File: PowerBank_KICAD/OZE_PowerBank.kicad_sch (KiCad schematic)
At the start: 86 parts, among them IC1 TPS2514ADBVT, IC3 TPS25810RVCR, J1 Conn_01x02_Pin, J10 Conn_01x04_Pin, J11 Conn_01x02_Pin, J12 Battery with BMS Input, J13 Conn_01x10_Pin, J2 DCJ200-10-A-XX-K_REVA, J3 Conn_01x04_Pin, J4 Conn_01x04_Pin, J5 Conn_01x04_Pin, J6 Conn_01x10_Pin, J7 USB_A, J8 USB_C_Receptacle_PowerOnly_6P, J9 Conn_01x04_Pin, Q1 PMOS, Q2 IRLZ44N, Q3 IRLZ44N, SW1 SW_Push, SW2 SW_SPDT, U1 TLV70233_SOT23-5, U2 STM32F103C8Tx, U3 LM5106SD, U5 INA180A2, Y1 16MHz

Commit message: added conectors footprints
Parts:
- added C33: 10u, Capacitor_SMD:C_0805_2012Metric_Pad1.18x1.45mm_HandSolder, symbol Device:C_Small
- added C34, C35: 100n, Capacitor_SMD:C_0805_2012Metric_Pad1.18x1.45mm_HandSolder, symbol Device:C_Small
- added D10: BLUE, LED_SMD:LED_1206_3216Metric_Pad1.42x1.75mm_HandSolder, symbol Device:LED
- added H1, H2, H3, H4: MountingHole, MountingHole:MountingHole_2.2mm_M2_ISO7380, symbol Mechanical:MountingHole
- added J14: Conn_01x04_Pin, symbol Connector:Conn_01x04_Pin
- added J15, J16, J17: Conn_01x04_Pin, Connector_PinSocket_2.54mm:PinSocket_1x04_P2.54mm_Vertical, symbol Connector:Conn_01x04_Pin
- added R17: 1k, Resistor_SMD:R_0805_2012Metric_Pad1.20x1.40mm_HandSolder, symbol Device:R
- added R18, R19, R25: 100k, Resistor_SMD:R_0805_2012Metric_Pad1.20x1.40mm_HandSolder, symbol Device:R
- added R20, R21, R22, R23, R24: 0, Resistor_SMD:R_0805_2012Metric_Pad1.20x1.40mm_HandSolder, symbol Device:R
- J1: footprint (none) -> TerminalBlock_Phoenix:TerminalBlock_Phoenix_PT-1,5-2-5.0-H_1x02_P5.00mm_Horizontal
- J10: footprint (none) -> TerminalBlock_Phoenix:TerminalBlock_Phoenix_PT-1,5-4-5.0-H_1x04_P5.00mm_Horizontal
- J11: footprint (none) -> Connector_JST:JST_XH_B2B-XH-A_1x02_P2.50mm_Vertical
- J13, J6: footprint (none) -> Connector_PinSocket_2.54mm:PinSocket_1x10_P2.54mm_Vertical
- J9: footprint (none) -> TerminalBlock_Phoenix:TerminalBlock_Phoenix_PT-1,5-4-3.5-H_1x04_P3.50mm_Horizontal
- U5: value INA180A2 -> INA180A1
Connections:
- net +12V: now also J17.3 (Pin_3), J17.4 (Pin_4)
- net +3.3V: now also IC3.5 (AUX), C33.1, C34.1, J14.3 (Pin_3), J14.4 (Pin_4), J15.3 (Pin_3), J15.4 (Pin_4), R18.2, R19.2, R25.2
- net +5V: now also J16.3 (Pin_3), J16.4 (Pin_4); no longer IC3.5 (AUX), IC3.6 (EN)
- net ENABLE: now also R20.2; no longer U2.10 (PA0)
- net GND: now also C33.2, C34.2, C35.2, D10.1 (K), J14.1 (Pin_1), J14.2 (Pin_2), J15.1 (Pin_1), J15.2 (Pin_2), J16.1 (Pin_1), J16.2 (Pin_2), J17.1 (Pin_1), J17.2 (Pin_2)
- net I_OUT: now also R24.2; no longer U2.14 (PA4)
- net PWM: now also R21.2; no longer U2.11 (PA1)
- net V_BAT: now also R23.2; no longer U2.13 (PA3)
- net V_beforeBUCK: now also R22.2; no longer U2.12 (PA2)
- net at C25.1, C26.1, C27.1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: now also IC3.15 (OUT-B)
- net at C28.1, C29.1, L1.2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: now also R17.2
- net at C12.1, C14.1, FB1.1: now also C35.1
- net FAULT: now reaches U2.31 (PA10)
- net FAULT: now also IC3.1 (~{FAULT}), R19.1
- net ENABLE_TPS: now reaches U2.32 (PA11)
- net ENABLE_TPS: now also IC3.6 (EN)
- net LD_DET: now reaches U2.33 (PA12)
- net LD_DET: now also IC3.20 (~{LD_DET}), R18.1
- net UFP: now reaches U2.38 (PA15)
- net UFP: now also IC3.19 (~{UFP}), R25.1
- net DM1 renamed D-
- net DP1 renamed D+
- new net: D10.2 (A), R17.1
- new net: R22.1, U2.12 (PA2)
- new net: R24.1, U2.14 (PA4)
- new net: R20.1, U2.10 (PA0)
- new net: R21.1, U2.11 (PA1)
- new net: R23.1, U2.13 (PA3)
- no-connect marks 21 -> 13
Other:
- note added: "1%tolerance"
- note added: "1x 100nF per VDD Pin"
- note added: "Brak UFP może wyłączyć przetwornicę"
- note added: "O Ohm to be modular, in case of failure with STM32"
- note added: "diferential pair"
- note added: "electrolytic or ceracmic?"
- note added: "linie CC bardzo krótkie"
- note added: "termal pad, multiple vias"
- note added: "zabezpieczenie żeby nie spalić portu ADC?"
- note added: "zmień na uniwerslane zielone złącze"
- note removed: "1x 100mF per VDD Pin"
- moved on the sheet: C15, C18, C19, C20, C21, FB1

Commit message: PCB layout
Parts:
- removed C24, C29: 150uF, symbol Device:C_Polarized
- removed Q1: PMOS, symbol Simulation_SPICE:PMOS
- added C21, C28: 865060657011, 865060657011:CAPAE1030X1050N, symbol 865060657011:865060657011
- added Q1: IRLML6402TRPBF, IRLML6402TRPBF:SOT95P237X112-3N, symbol IRLML6402TRPBF:IRLML6402TRPBF
- 100k1, FB1: footprint (none) -> Resistor_SMD:R_0603_1608Metric_Pad0.98x0.95mm_HandSolder
- C11, C3, C6, C7, C8, C9: footprint Capacitor_SMD:C_0805_2012Metric_Pad1.18x1.45mm_HandSolder -> Capacitor_SMD:C_0402_1005Metric
- C13: footprint Capacitor_SMD:C_0603_1608Metric_Pad1.08x0.95mm_HandSolder -> Capacitor_SMD:C_0402_1005Metric
- C15: renamed from C35; footprint Capacitor_SMD:C_0805_2012Metric_Pad1.18x1.45mm_HandSolder -> Capacitor_SMD:C_0402_1005Metric
- C27: renamed from C34; footprint Capacitor_SMD:C_0805_2012Metric_Pad1.18x1.45mm_HandSolder -> Capacitor_SMD:C_0402_1005Metric
- C30: renamed from C32; footprint Capacitor_SMD:C_0805_2012Metric_Pad1.18x1.45mm_HandSolder -> Capacitor_SMD:C_0402_1005Metric
- D4: value 10V -> SZMM3Z10VST1G; footprint Diode_SMD:D_MiniMELF -> Diode_SMD:D_SOD-323
- J10: renamed from J7; footprint (none) -> Connector_USB:USB_A_TE_292303-7_Horizontal
- J17: renamed from J12; footprint (none) -> TerminalBlock_Phoenix:TerminalBlock_Phoenix_PT-1,5-2-5.0-H_1x02_P5.00mm_Horizontal
- J3, J4, J5: footprint (none) -> Connector_PinSocket_2.54mm:PinSocket_1x04_P2.54mm_Vertical
- J6: renamed from J14; footprint (none) -> Connector_PinSocket_2.54mm:PinSocket_1x04_P2.54mm_Vertical
- J9: renamed from J8; footprint (none) -> Connector_USB:USB_C_Receptacle_GCT_USB4125-xx-x-0190_6P_TopMnt_Horizontal
- L1: footprint (none) -> Inductor_SMD:L_Pulse_PA4320
- R15: renamed from R10; footprint Resistor_SMD:R_0805_2012Metric_Pad1.20x1.40mm_HandSolder -> Resistor_SMD:R_0402_1005Metric
- R19: renamed from R25; footprint Resistor_SMD:R_0805_2012Metric_Pad1.20x1.40mm_HandSolder -> Resistor_SMD:R_0402_1005Metric
- R20: renamed from R18; footprint Resistor_SMD:R_0805_2012Metric_Pad1.20x1.40mm_HandSolder -> Resistor_SMD:R_0402_1005Metric
- R21: renamed from R19; footprint Resistor_SMD:R_0805_2012Metric_Pad1.20x1.40mm_HandSolder -> Resistor_SMD:R_0402_1005Metric
- SW1: footprint (none) -> Button_Switch_THT:SW_PUSH-12mm_Wuerth-430476085716
- U3: now not fitted
- Y1: footprint (none) -> LFXTAL071744Reel:LFXTAL071744Reel
- renumbered C15 to C16, C16 to C17, C17 to C18, C22 to C19, C23 to C20, C18 to C22, C19 to C23, C20 to C24, C33 to C25, C21 to C26, C28 to C29, C26 to C31, C27 to C32, C25 to C33, C30 to C34, C31 to C35, D9 to D10, D10 to D8, D8 to D9, IC3 to IC1, IC1 to IC2, J9 to J11, J10 to J12, J15 to J13, J16 to J14, J17 to J15, J11 to J16, J6 to J7, J13 to J8, R2 to R1, R23 to R10, R24 to R11, R7 to R12, R8 to R13, R9 to R14, R11 to R16, R12 to R17, R13 to R18, R3 to R2, R17 to R22, R14 to R23, R15 to R24, R16 to R25, R1 to R3, R20 to R7, R21 to R8, R22 to R9, U5 to U4
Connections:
- net GND: now also C31.1, C21.2 (-), C28.2 (-); no longer C31.2
- net VIN: now also C21.1 (+), Q1.2 (S)
- net VBUS: now reaches C32.1, C33.1, IC1.14 (OUT-A), IC1.15 (OUT-B), IC2.5 (IN), J10.1 (VBUS), J9.A9 (VBUS), J9.B9 (VBUS)
- net VBUS: now also C31.2; no longer C31.1
- net Gate: now reaches D4.2 (A), R12.1
- net Gate: now also Q1.1 (G)
- net at C29.1, L1.2, R22.2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: now also C28.1 (+)
- net DREN: now reaches D3.2 (A2), F1.2
- net DREN: now also Q1.3 (D)
- no-connect marks 13 -> 16
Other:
- note added: "STEP DOWN"
- note added: "STEP UP"
- moved on the sheet: C29, C31, R12

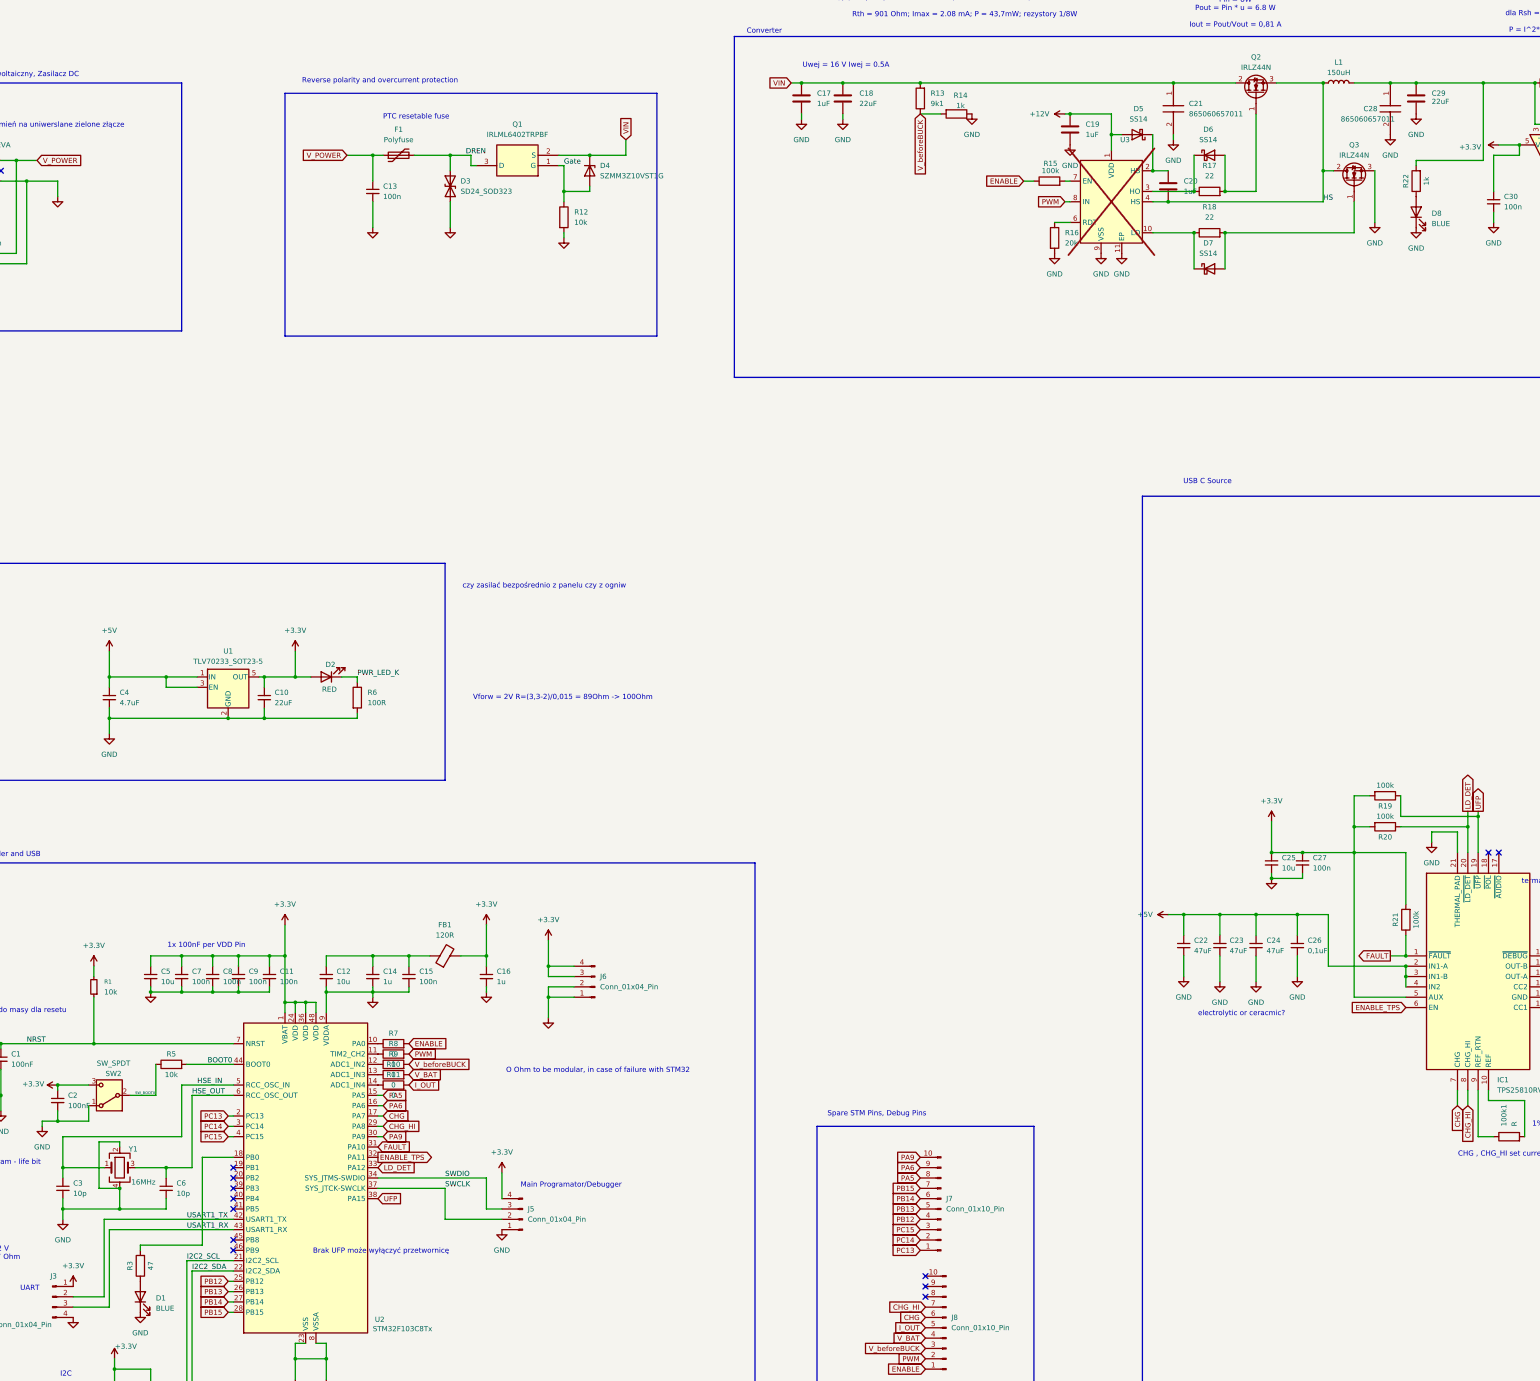
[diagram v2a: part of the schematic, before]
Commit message: 26.11 Hubert - PCB
Poprowadzone ścieżki sygnałowe, prądowe, poza 2 wchodzącymi do sterownika USB-C, USB-A . Brak wylanej masy
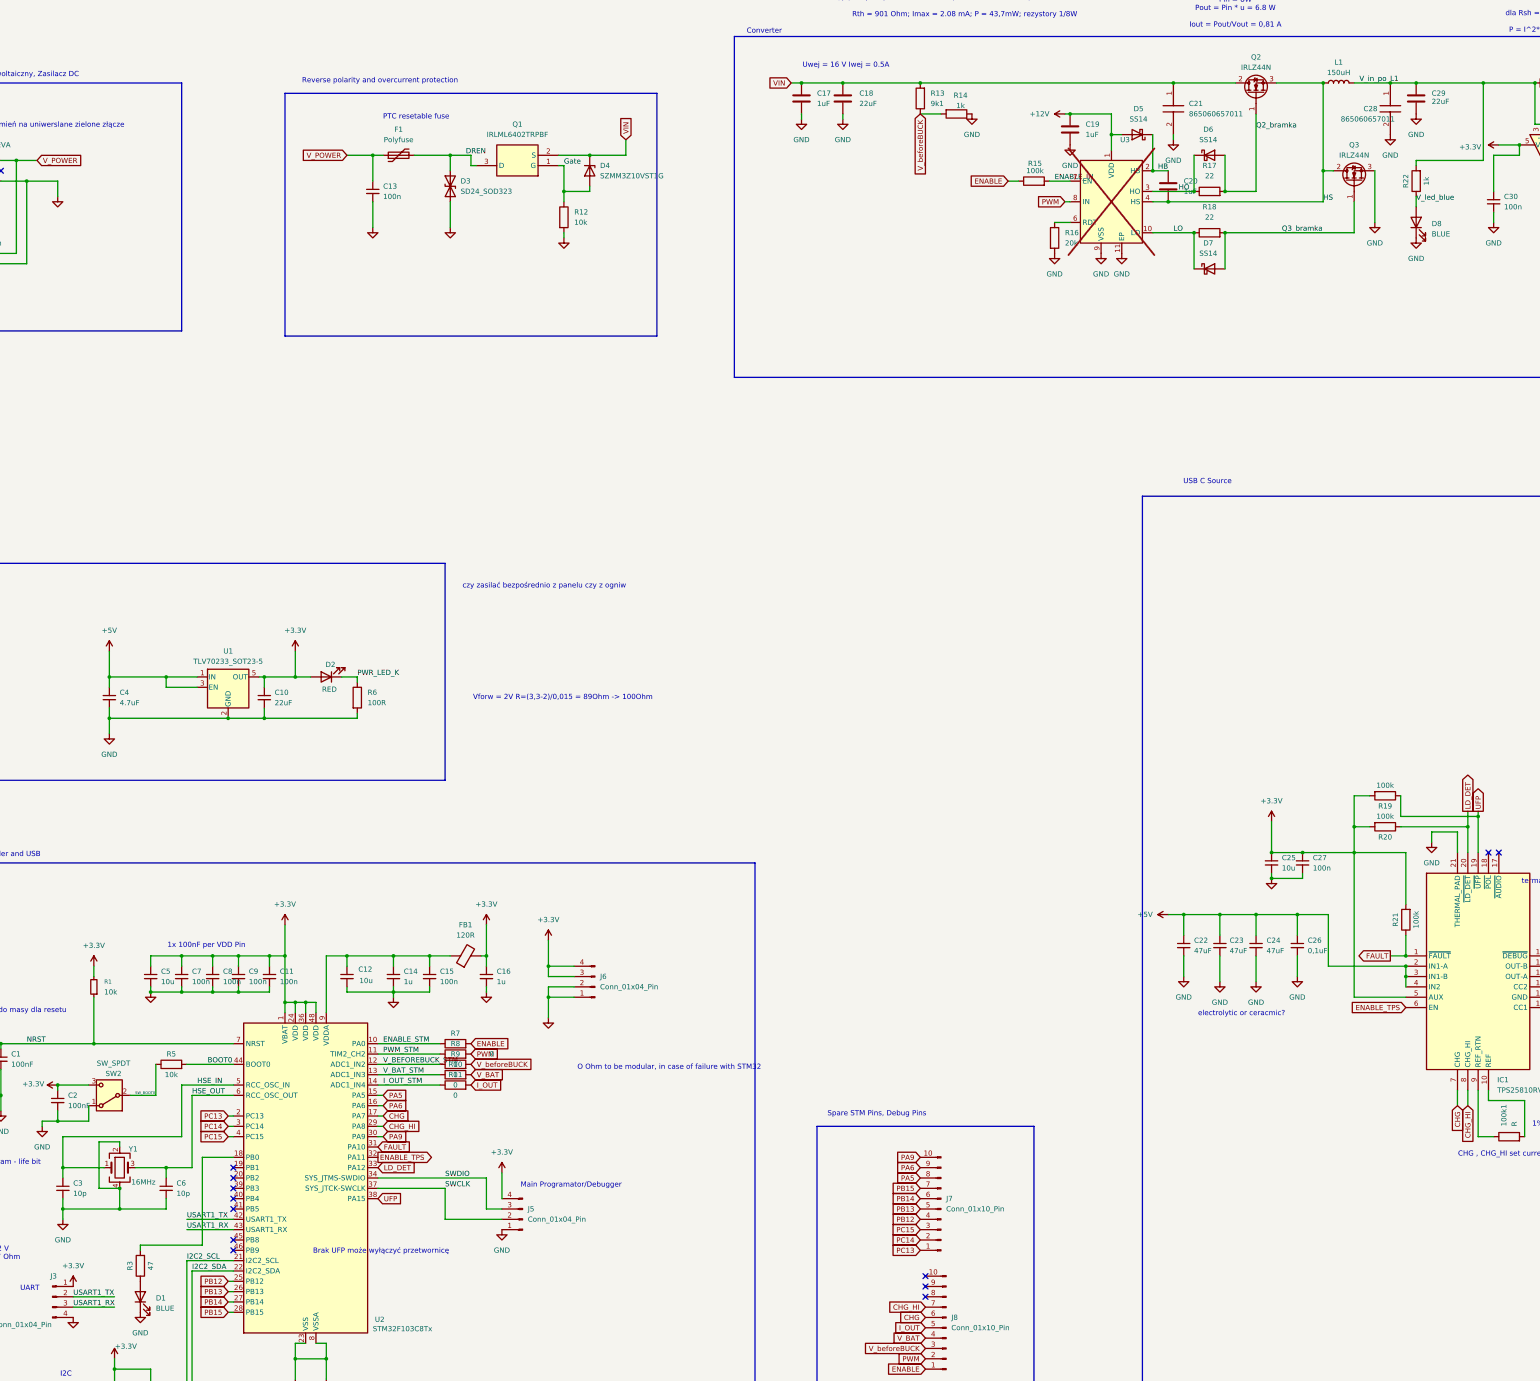
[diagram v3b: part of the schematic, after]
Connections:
- net GND: no longer U2.9 (VDDA)
- net at C12.1, C14.1, C15.1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: now also U2.9 (VDDA)
- net V_led_blue: now reaches D8.2 (A), R22.1
- net HB: now reaches C20.1, D5.1 (K), U3.2 (HB)
- net V_in_po_L1: now reaches C28.1 (+), C29.1, L1.2, R22.2, R23.1, U4.3 (+)
- net Q3_bramka: now reaches D7.2 (A), Q3.1 (G), R18.2
- net HO: now reaches D6.1 (K), R17.1, U3.3 (HO)
- net Q2_bramka: now reaches D6.2 (A), Q2.1 (G), R17.2
- net V_BEFOREBUCK_STM: now reaches R9.1, U2.12 (PA2)
- net I_OUT_STM: now reaches R11.1, U2.14 (PA4)
- net LO: now reaches D7.1 (K), R18.1, U3.10 (LO)
- net ENABLE_IN: now reaches R15.2, U3.7 (EN)
- net ENABLE_STM: now reaches R7.1, U2.10 (PA0)
- net PWM_STM: now reaches R8.1, U2.11 (PA1)
- net V_BAT_STM: now reaches R10.1, U2.13 (PA3)
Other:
- moved on the sheet: C12, C14, C15, D8, FB1, R10, R11, R15, R7, R8, R9

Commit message: changed footprint, correct GND conection to thermal, remove some vias, give additional vias in TPS25810
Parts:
- C1, C2: footprint Capacitor_SMD:C_0805_2012Metric_Pad1.18x1.45mm_HandSolder -> PCM_JLCPCB:C_0805; symbol Device:C_Small -> PCM_JLCPCB-Capacitors:0805,100nF; Attrition Qty (none) -> 10; Capacitance (none) -> 100nF; Category (none) -> Capacitors,Multilayer Ceramic Capacitors MLCC - SMD/SMT; Class (none) -> Basic Component; LCSC (none) -> C28233; Manufacturer (none) -> Samsung Electro-Mechanics; Minimum Qty (none) -> 20; Part (none) -> CL21B104KCFNNNE; Price (none) -> 0.009USD; Process (none) -> SMT; Stock (none) -> 1168020; Temperature Coefficient (none) -> X7R; Tolerance (none) -> ±10%; Voltage Rated (none) -> 100V
- C11, C15, C27, C30, C7, C8, C9: footprint Capacitor_SMD:C_0402_1005Metric -> PCM_JLCPCB:C_0402; symbol Device:C_Small -> PCM_JLCPCB-Capacitors:0402,100nF; Attrition Qty (none) -> 10; Capacitance (none) -> 100nF; Category (none) -> Capacitors,Multilayer Ceramic Capacitors MLCC - SMD/SMT; Class (none) -> Basic Component; LCSC (none) -> C1525; Manufacturer (none) -> Samsung Electro-Mechanics; Minimum Qty (none) -> 20; Part (none) -> CL05B104KO5NNNC; Price (none) -> 0.004USD; Process (none) -> SMT; Stock (none) -> 20208285; Temperature Coefficient (none) -> X7R; Tolerance (none) -> ±10%; Voltage Rated (none) -> 16V
- C12, C25, C31, C32: footprint Capacitor_SMD:C_0805_2012Metric_Pad1.18x1.45mm_HandSolder -> PCM_JLCPCB:C_0805; symbol Device:C_Small -> PCM_JLCPCB-Capacitors:0805,10uF; Attrition Qty (none) -> 10; Capacitance (none) -> 10uF; Category (none) -> Capacitors,Multilayer Ceramic Capacitors MLCC - SMD/SMT; Class (none) -> Basic Component; LCSC (none) -> C15850; Manufacturer (none) -> Samsung Electro-Mechanics; Minimum Qty (none) -> 20; Part (none) -> CL21A106KAYNNNE; Price (none) -> 0.014USD; Process (none) -> SMT; Stock (none) -> 6525809; Temperature Coefficient (none) -> X5R; Tolerance (none) -> ±10%; Voltage Rated (none) -> 25V
- C13: footprint Capacitor_SMD:C_0402_1005Metric -> Capacitor_SMD:C_0805_2012Metric
- C14, C16, C26, C33: footprint Capacitor_SMD:C_0805_2012Metric_Pad1.18x1.45mm_HandSolder -> PCM_JLCPCB:C_0805; symbol Device:C_Small -> PCM_JLCPCB-Capacitors:0805,1uF; Attrition Qty (none) -> 10; Capacitance (none) -> 1uF; Category (none) -> Capacitors,Multilayer Ceramic Capacitors MLCC - SMD/SMT; Class (none) -> Basic Component; LCSC (none) -> C28323; Manufacturer (none) -> Samsung Electro-Mechanics; Minimum Qty (none) -> 20; Part (none) -> CL21B105KBFNNNE; Price (none) -> 0.012USD; Process (none) -> SMT; Stock (none) -> 4334256; Temperature Coefficient (none) -> X7R; Tolerance (none) -> ±10%; Voltage Rated (none) -> 50V
- C17, C19: footprint Capacitor_SMD:C_0805_2012Metric_Pad1.18x1.45mm_HandSolder -> PCM_JLCPCB:C_0805; symbol Device:C -> PCM_JLCPCB-Capacitors:0805,1uF; Attrition Qty (none) -> 10; Capacitance (none) -> 1uF; Category (none) -> Capacitors,Multilayer Ceramic Capacitors MLCC - SMD/SMT; Class (none) -> Basic Component; LCSC (none) -> C28323; Manufacturer (none) -> Samsung Electro-Mechanics; Minimum Qty (none) -> 20; Part (none) -> CL21B105KBFNNNE; Price (none) -> 0.012USD; Process (none) -> SMT; Stock (none) -> 4334256; Temperature Coefficient (none) -> X7R; Tolerance (none) -> ±10%; Voltage Rated (none) -> 50V
- C3, C6: footprint Capacitor_SMD:C_0402_1005Metric -> PCM_JLCPCB:C_0402; symbol Device:C_Small -> PCM_JLCPCB-Capacitors:0402,10pF; Attrition Qty (none) -> 10; Capacitance (none) -> 10pF; Category (none) -> Capacitors,Multilayer Ceramic Capacitors MLCC - SMD/SMT; Class (none) -> Basic Component; LCSC (none) -> C32949; Manufacturer (none) -> Samsung Electro-Mechanics; Minimum Qty (none) -> 20; Part (none) -> CL05C100JB5NNNC; Price (none) -> 0.007USD; Process (none) -> SMT; Stock (none) -> 564575; Temperature Coefficient (none) -> C0G; Tolerance (none) -> ±5%; Voltage Rated (none) -> 50V
- R10, R11, R7, R8, R9: footprint Resistor_SMD:R_0805_2012Metric_Pad1.20x1.40mm_HandSolder -> PCM_JLCPCB:R_0805; symbol Device:R -> PCM_JLCPCB-Resistors:0805,0Ω; Attrition Qty (none) -> 10; Category (none) -> Resistors,Chip Resistor - Surface Mount; Class (none) -> Basic Component; LCSC (none) -> C17477; Manufacturer (none) -> UNI-ROYAL(Uniroyal Elec); Minimum Qty (none) -> 20; Operating Temperature Range (none) -> -55°C~+155°C; Overload Voltage (Max) (none) -> 150V; Part (none) -> 0805W8F0000T5E; Power(Watts) (none) -> 125mW; Price (none) -> 0.005USD; Process (none) -> SMT; Resistance (none) -> 0Ω; Stock (none) -> 7792489; Temperature Coefficient (none) -> ±800ppm/°C; Tolerance (none) -> ±1%; Type (none) -> Thick Film Resistors
- U3: now fitted
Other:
- note added: "Na wyższe U"
- moved on the sheet: C32, C33
